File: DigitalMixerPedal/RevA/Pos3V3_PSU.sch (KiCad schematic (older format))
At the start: 7 parts, among them U2 MCP1703A-3302_SOT223

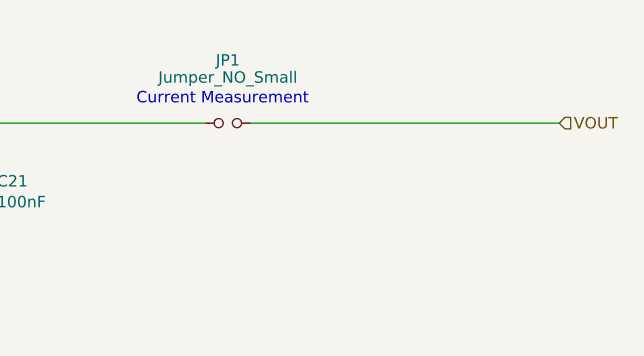
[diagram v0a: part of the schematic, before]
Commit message: updated hw
- added testpoints
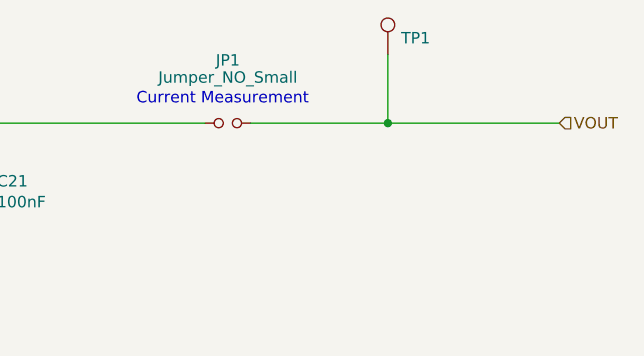
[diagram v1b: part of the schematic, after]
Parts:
- added TP1: TestPoint, TestPoint:TestPoint_Pad_D1.0mm, symbol Connector:TestPoint
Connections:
- net VOUT: now also TP1.1
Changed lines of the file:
@@
 	4100 3125 3600 3125
 Wire Wire Line
-	7325 2425 8675 2425
+	7325 2425 7925 2425
 $Comp
 L Regulator_Linear:MCP1703A-3302_SOT223 U2
@@
 	1    0    0    -1
 $EndComp
+$Comp
+L Connector:TestPoint TP?
+U 1 1 5F7288CE
+P 7925 2125
+AR Path="/5F6E135D/5F7288CE" Ref="TP?"  Part="1"
+AR Path="/5F6E91E5/5F7288CE" Ref="TP?"  Part="1"
+AR Path="/5F6EDB29/5F7288CE" Ref="TP?"  Part="1"
+AR Path="/5F6F225F/5F7288CE" Ref="TP?"  Part="1"
+AR Path="/5F74C2DC/5F7288CE" Ref="TP?"  Part="1"
+AR Path="/5F3902BC/5F7288CE" Ref="TP1"  Part="1"
+F 0 "TP1" H 7983 2197 50  0000 L CNN
+F 1 "TestPoint" H 7983 2152 50  0001 L CNN
+F 2 "TestPoint:TestPoint_Pad_D1.0mm" H 8125 2125 50  0001 C CNN
+F 3 "~" H 8125 2125 50  0001 C CNN
+	1    7925 2125
+	1    0    0    -1
+$EndComp
+Wire Wire Line
+	7925 2125 7925 2425
+Connection ~ 7925 2425
+Wire Wire Line
+	7925 2425 8675 2425
 $EndSCHEMATC
